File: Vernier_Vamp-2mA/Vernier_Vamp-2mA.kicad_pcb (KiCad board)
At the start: 4 copper layers, 128.5 x 99.5 mm, 185 parts, among them J1 Conn_01x02, J2 RJ45, J3 Screw_Terminal_01x04, J4 Conn_02x07_Odd_Even, J5 Conn_Coaxial, J6 Conn_Coaxial, J7 Conn_Coaxial, Q1 Si4447ADY, Q2 IRF8707PbF, SW1 DPDT_Hirose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

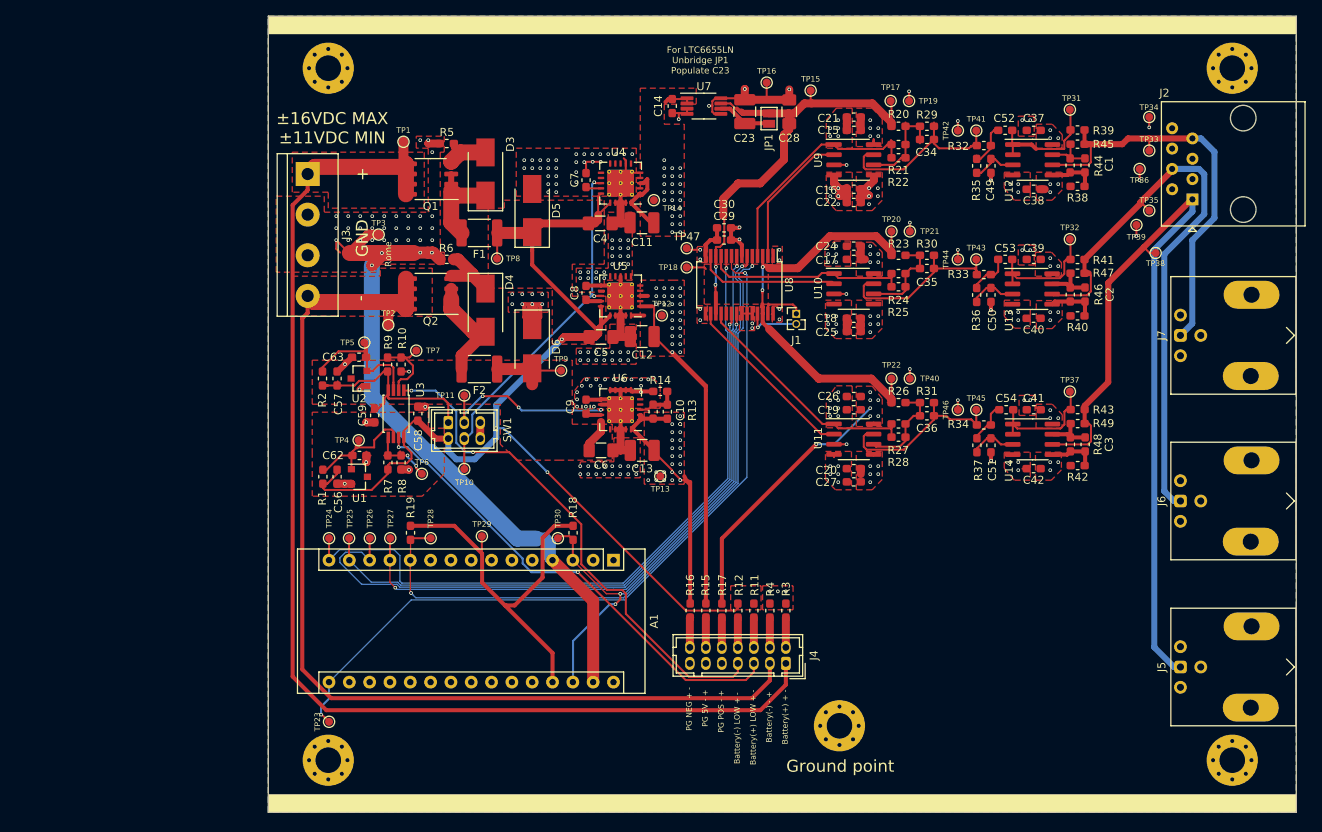
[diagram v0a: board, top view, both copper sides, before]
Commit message: Applied 1.0B changes to 2mA version
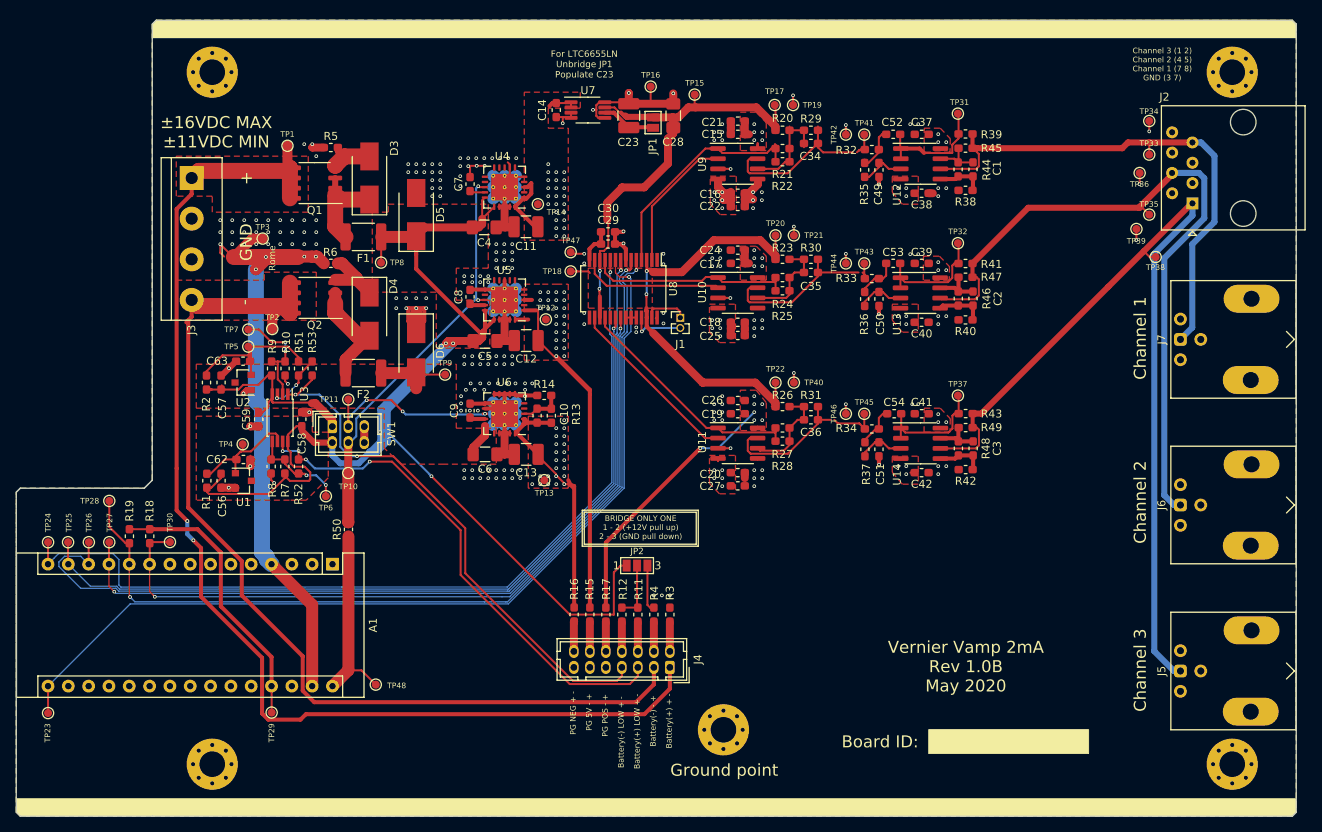
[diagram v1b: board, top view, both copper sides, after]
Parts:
- added JP2: SolderJumper_3_Open, Jumper:SolderJumper-3_P1.3mm_Open_Pad1.0x1.5mm_NumberLabels, F.Cu at (110.5, 115.3)
- added R50: 0R, Resistor_SMD:R_0603_1608Metric_Pad1.05x0.95mm_HandSolder, F.Cu at (74.4, 110.8)
- added R51: 3k, Resistor_SMD:R_0603_1608Metric_Pad1.05x0.95mm_HandSolder, F.Cu at (68.2, 90.7)
- added R52: 2M, Resistor_SMD:R_0603_1608Metric_Pad1.05x0.95mm_HandSolder, F.Cu at (68.2, 102.9)
- added R53: 133k, Resistor_SMD:R_0603_1608Metric_Pad1.05x0.95mm_HandSolder, F.Cu at (69.9, 90.7)
- added TP48: TestPoint_Probe, TestPoint:TestPoint_Pad_D1.0mm, F.Cu at (77.8, 130.2)
- J5: value Conn_Coaxial -> Channel 3
- J6: value Conn_Coaxial -> Channel 2
- J7: value Conn_Coaxial -> Channel 1
- R9: value 120k -> 133k
- moved R18 52.9 mm to (49.6, 111.7)
- moved TP30 48.5 mm to (52.1, 112.4)
- moved TP28 40.4 mm to (44.5, 107.2), turned to 0 degrees
- moved TP23 35.1 mm to (36.9, 133.8)
- moved R19 35.1 mm to (47.0, 111.7)
- moved TP27 35.1 mm to (44.5, 112.4)
- moved A1 35.1 mm to (72.4, 115.2)
- moved TP24 35.1 mm to (36.9, 112.4)
- moved TP25 35.1 mm to (39.4, 112.4)
- moved TP26 35.1 mm to (42.0, 112.4)
- moved TP29 34.3 mm to (64.8, 133.7)
- moved TP7 21.2 mm to (61.9, 85.8), turned to 180 degrees
- moved R8 16.2 mm to (64.8, 102.9)
- moved C58 14.5 mm to (68.6, 97.0)
- moved C15 14.5 mm to (123.1, 61.4)
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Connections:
- net +8V renamed +7V5
- net -8V renamed -7V5
- net /Power/+5V_c_ref renamed /Power/Battery_Management/+5V_c_ref
- net /Power/+EN renamed +12V_batt_post
- net /Power/LED1_N renamed /Power/Battery_Management/Battery+_C
- net /Power/LED2_P renamed /Power/Battery_Management/Battery-_A
- net /Power/LED3_N renamed /Power/Battery_Management/Battery+_LOW_C
- net /Power/LED3_P renamed /Power/Battery_Management/Battery+_LOW_A
- net /Power/LED4_N renamed /Power/Battery_Management/Battery-_LOW_C
- net /Power/LED4_P renamed /Power/Battery_Management/Battery-_LOW_A
- net /Power/LED5_P renamed /Power/Battery_Management/+7.5_PG_A
- net /Power/LED6_P renamed /Power/Battery_Management/+5_PG_A
- net /Power/LED7_N renamed /Power/Battery_Management/-7.5_PG_C
- A1 pad 10: Net-(A1-Pad10) -> /DAC/~RS
- A1 pad 28: /DAC/~RS -> Net-(A1-Pad28)
- A1 pad 3: /DAC/~RS -> Net-(A1-Pad3)
- C63 pad 1: /Power/-5V_c_ref -> /Power/Battery_Management/-5V_c_ref
- R11 pad 1: /Power/+12VDC_bat -> Net-(JP2-Pad2)
- R12 pad 1: /Power/+12VDC_bat -> Net-(JP2-Pad2)
- R2 pad 1: /Power/-5V_c_ref -> /Power/Battery_Management/-5V_c_ref
- TP5 pad 1: /Power/-5V_c_ref -> /Power/Battery_Management/-5V_c_ref
- U2 pad 2: /Power/-5V_c_ref -> /Power/Battery_Management/-5V_c_ref
- U3 pad 3: /Power/-5V_c_ref -> Net-(R51-Pad1)
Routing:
- net GND: track 156.2 -> 203.7 mm
- net /Power/+12VDC_bat: track 143.0 -> 172.8 mm, vias 3 -> 4
- net /DAC/~RS: track 76.1 -> 103.1 mm, vias 3 -> 2
- net Net-(A1-Pad30): track 0.00 -> 26.5 mm
- net /DAC/MSB: track 86.3 -> 111.2 mm
- net /DAC/SDO: track 78.0 -> 98.6 mm
- net /DAC/SDI: track 90.2 -> 110.8 mm
- net /DAC/~LDAC: track 75.6 -> 96.3 mm
- net /DAC/~CS: track 91.9 -> 112.5 mm
- net /Power/Battery_Management/-5V_c_ref: track 0.00 -> 18.4 mm
- net /Power/-5V_c_ref: track 18.4 -> 0.00 mm
- net /DAC/CLK: track 97.8 -> 116.0 mm, vias 2 -> 1
- net /Channel_Outputs/Coil_Iout_2: track 76.0 -> 90.0 mm
- net /Channel_Outputs/Coil_Iout_1: track 54.1 -> 68.1 mm
- net +5VD: track 47.8 -> 35.4 mm
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- added copper zone on F.Cu, net (none)
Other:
- board size 128.5 x 99.5 mm -> 160 x 99.5 mm
- board text added: "BRIDGE ONLY ONE 1 - 2 (+12V pull up) 2 - 3 (GND pull down)"
- board text added: "Board ID:"
- board text added: "Channel 1"
- board text added: "Channel 2"
- board text added: "Channel 3"
- board text added: "Channel 3 (1 2) Channel 2 (4 5) Channel 1 (7 8) GND (3 7)"
- board text added: "Vernier Vamp 2mA Rev 1.0B May 2020"
- board text added: "Vernier Vamp 2mA Rev 1.0B May 2020 Designer: Marcin Mrozowski EQOP"
- board text removed: "Vernier Vamp 200mA Rev 1.0A EQOP"

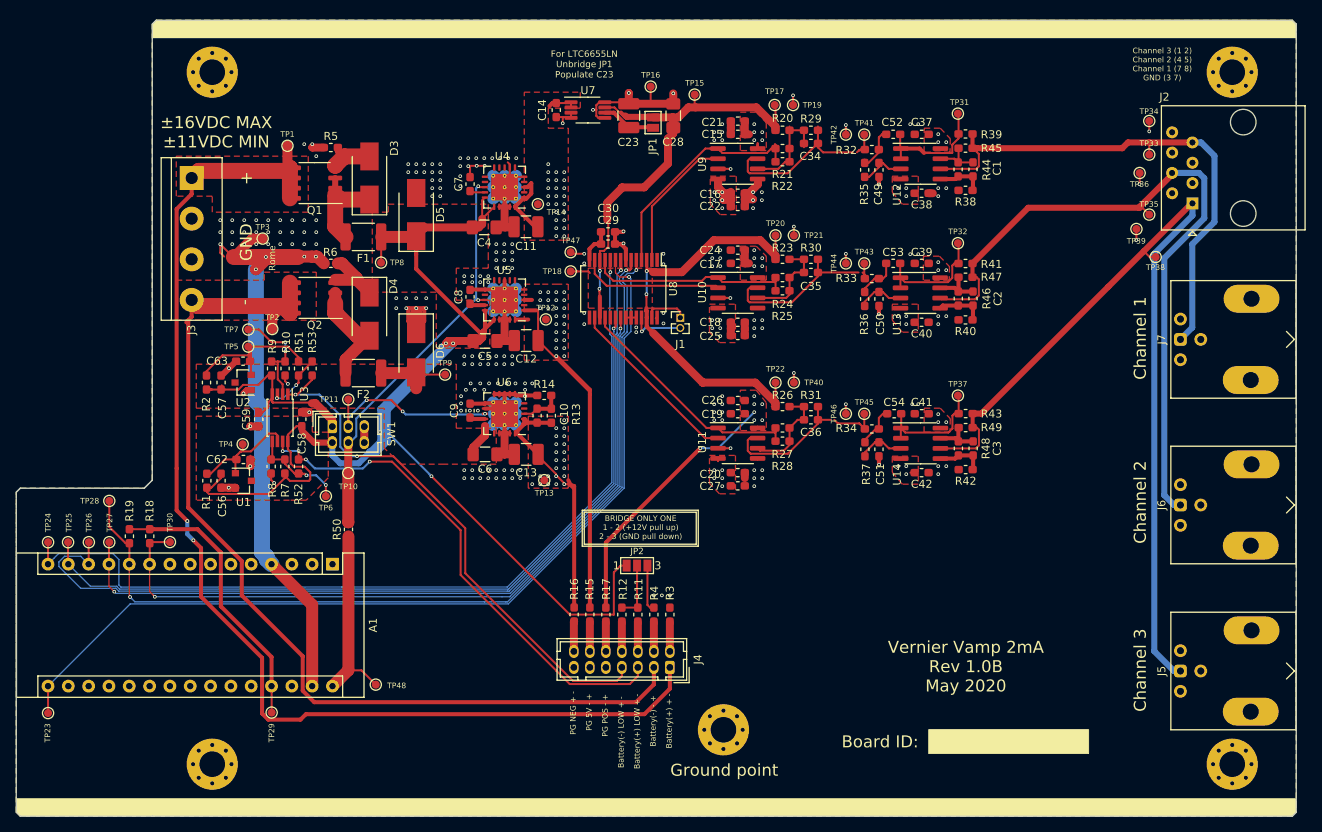
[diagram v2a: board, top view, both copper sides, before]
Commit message: 1.0C Initial commit
-Fixed amplifier output
-Changed connectors to IDC
-Via perimeter added
TODO:
Add shielding over analogue section
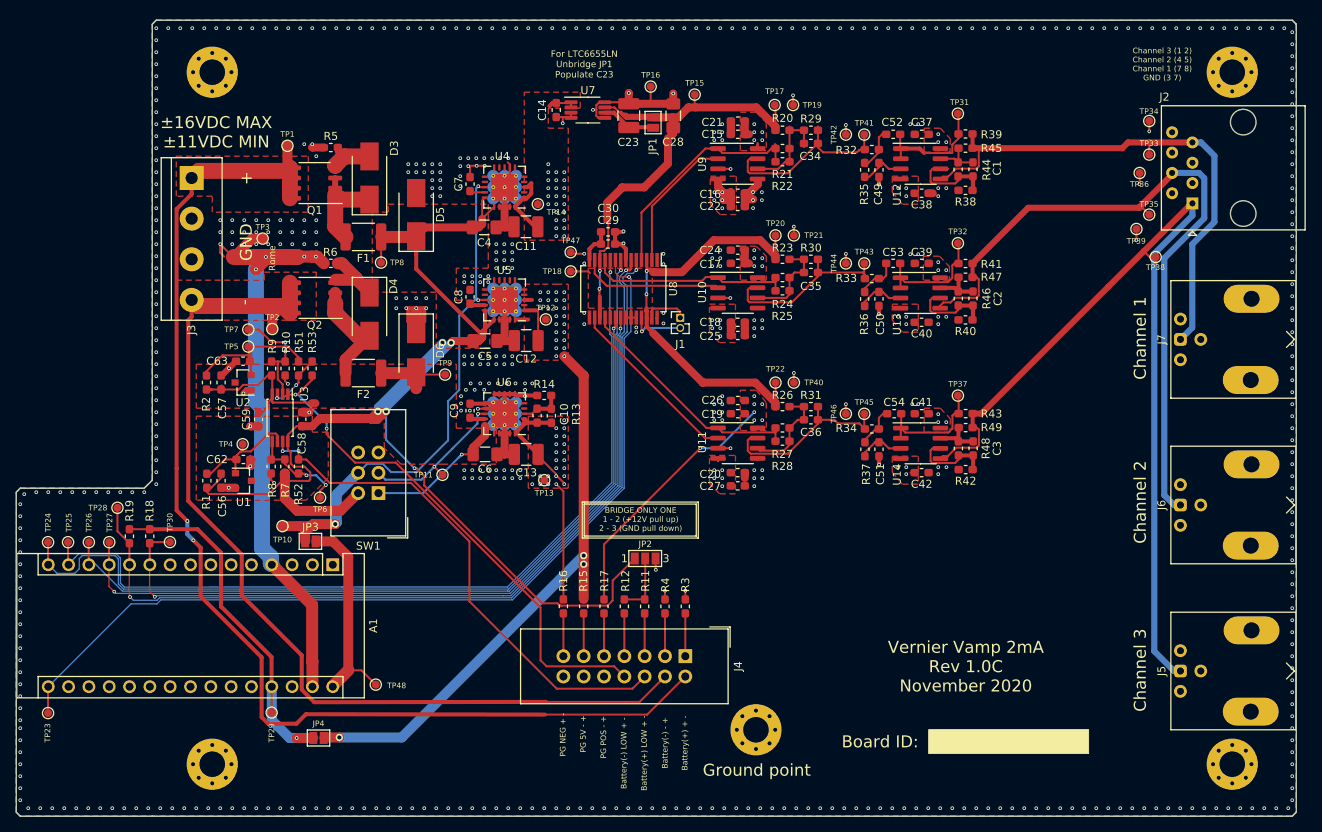
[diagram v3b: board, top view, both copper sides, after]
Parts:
- removed R50: 0R, Resistor_SMD:R_0603_1608Metric_Pad1.05x0.95mm_HandSolder
- added JP3: SolderJumper_2_Open, Jumper:SolderJumper-2_P1.3mm_Open_Pad1.0x1.5mm, F.Cu at (69.7, 112.3)
- added JP4: SolderJumper_2_Open, Jumper:SolderJumper-2_P1.3mm_Open_Pad1.0x1.5mm, F.Cu at (70.7, 136.9)
- A1: value Arduino_Nano_v3.x -> Arduino_Nano_Every
- J4: footprint Connector_Hirose:Hirose_DF11-14DP-2DSA_2x07_P2.00mm_Vertical -> Connector_IDC:IDC-Header_2x07_P2.54mm_Vertical
- SW1: footprint Connector_Hirose:Hirose_DF11-6DP-2DSA_2x03_P2.00mm_Vertical -> Connector_IDC:IDC-Header_2x03_P2.54mm_Vertical
- moved TP11 15.1 mm to (86.2, 104.0)
- moved TP10 10.6 mm to (66.2, 110.4)
- moved SW1 10.1 mm to (78.2, 106.3), turned to 180 degrees
- moved H5 4.06 mm to (125.4, 135.8)
- moved J4 2.39 mm to (116.5, 126.6), turned to 270 degrees
- moved R3 2.19 mm to (116.5, 120.4)
- moved R4 1.73 mm to (114.0, 120.4)
- moved R16 1.69 mm to (101.3, 120.4)
- moved JP2 1.35 mm to (111.5, 114.4)
- moved TP28 1.33 mm to (45.5, 108.1)
- moved R11 1.33 mm to (111.4, 120.4)
- moved R15 1.28 mm to (103.8, 120.4)
- moved R12 1.07 mm to (108.9, 120.4)
- moved R17 1.05 mm to (106.4, 120.4)
- moved TP6 0.75 mm to (70.9, 106.8)
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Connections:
- A1 pad 1: Net-(A1-Pad1) -> (no net)
- A1 pad 14: /DAC/SDO -> /DAC/SDI
- A1 pad 15: /DAC/SDI -> /DAC/SDO
- A1 pad 17: Net-(A1-Pad17) -> (no net)
- A1 pad 18: Net-(A1-Pad18) -> (no net)
- A1 pad 19: Net-(A1-Pad19) -> (no net)
- A1 pad 2: Net-(A1-Pad2) -> (no net)
- A1 pad 20: Net-(A1-Pad20) -> (no net)
- A1 pad 21: Net-(A1-Pad21) -> (no net)
- A1 pad 22: Net-(A1-Pad22) -> (no net)
- A1 pad 23: Net-(A1-Pad23) -> (no net)
- A1 pad 24: Net-(A1-Pad24) -> (no net)
- A1 pad 25: Net-(A1-Pad25) -> (no net)
- A1 pad 26: Net-(A1-Pad26) -> (no net)
- A1 pad 28: Net-(A1-Pad28) -> (no net)
- A1 pad 3: Net-(A1-Pad3) -> (no net)
- A1 pad 5: Net-(A1-Pad5) -> (no net)
- A1 pad 6: Net-(A1-Pad6) -> (no net)
- A1 pad 7: Net-(A1-Pad7) -> (no net)
- A1 pad 8: Net-(A1-Pad8) -> (no net)
- A1 pad 9: Net-(A1-Pad9) -> (no net)
- J4 pad 1: +BATT -> /Power/Battery_Management/Battery+_C
- J4 pad 10: /Power/Battery_Management/+7.5_PG_A -> GND
- J4 pad 11: GND -> /Power/Battery_Management/+5_PG_A
- J4 pad 12: /Power/Battery_Management/+5_PG_A -> GND
- J4 pad 13: GND -> /Power/Battery_Management/-7.5_PG_C
- J4 pad 14: /Power/Battery_Management/-7.5_PG_C -> GND
- J4 pad 2: /Power/Battery_Management/Battery+_C -> +BATT
- J4 pad 3: -BATT -> /Power/Battery_Management/Battery-_A
- J4 pad 4: /Power/Battery_Management/Battery-_A -> -BATT
- J4 pad 5: /Power/Battery_Management/Battery+_LOW_C -> /Power/Battery_Management/Battery+_LOW_A
- J4 pad 6: /Power/Battery_Management/Battery+_LOW_A -> /Power/Battery_Management/Battery+_LOW_C
- J4 pad 7: /Power/Battery_Management/Battery-_LOW_C -> /Power/Battery_Management/Battery-_LOW_A
- J4 pad 8: /Power/Battery_Management/Battery-_LOW_A -> /Power/Battery_Management/Battery-_LOW_C
- J4 pad 9: GND -> /Power/Battery_Management/+7.5_PG_A
- TP24 pad 1: /DAC/SDI -> /DAC/SDO
- TP25 pad 1: /DAC/SDO -> /DAC/SDI
- U12 pad 5: Net-(C1-Pad2) -> /Channel_Outputs/Coil_Iout_1
- U12 pad 6: /Channel_Outputs/Coil_Iout_1 -> Net-(C1-Pad2)
- U13 pad 5: Net-(C2-Pad2) -> /Channel_Outputs/Coil_Iout_2
- U13 pad 6: /Channel_Outputs/Coil_Iout_2 -> Net-(C2-Pad2)
- U14 pad 5: Net-(C3-Pad2) -> /Channel_Outputs/Coil_Iout_3
- U14 pad 6: /Channel_Outputs/Coil_Iout_3 -> Net-(C3-Pad2)
- U4 pad 10: Net-(U4-Pad10) -> GND
- U4 pad 11: GND -> (no net)
- U4 pad 4: Net-(U4-Pad4) -> (no net)
- U4 pad 5: GND -> (no net)
- U4 pad 6: Net-(U4-Pad6) -> GND
- U4 pad 8: Net-(U4-Pad8) -> GND
- U5 pad 10: Net-(U5-Pad10) -> GND
- U5 pad 11: GND -> (no net)
- U5 pad 12: Net-(U5-Pad12) -> (no net)
- U5 pad 4: Net-(U5-Pad4) -> (no net)
- U5 pad 5: Net-(U5-Pad5) -> (no net)
- U5 pad 8: GND -> (no net)
- U5 pad 9: Net-(U5-Pad9) -> (no net)
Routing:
- net +5V: track 57.2 -> 87.8 mm, vias 26 -> 29
- net +12V_batt_post: track 51.1 -> 65.7 mm, vias 2 -> 3
- net +5VD: track 35.4 -> 45.7 mm, vias 0 -> 1
- net GND: track 203.7 -> 193.8 mm, vias 225 -> 566
- net /Power/+12VDC_bat: track 172.8 -> 182.7 mm, vias 4 -> 5
- net /DAC/~CS: track 112.5 -> 104.0 mm
- net /DAC/SDO: track 98.6 -> 105.5 mm
- net /Power/-12VDC_bat: track 44.2 -> 50.6 mm, vias 0 -> 1
- net Net-(C1-Pad2): track 6.51 -> 12.0 mm
- net Net-(C3-Pad2): track 6.05 -> 10.6 mm
- net Net-(C2-Pad2): track 6.07 -> 10.6 mm
- net /Power/-EN: track 23.3 -> 19.2 mm, vias 3 -> 2
- net -7V5: track 40.6 -> 37.6 mm
- net /DAC/SDI: track 110.8 -> 108.3 mm
- net Net-(A1-Pad30): track 26.5 -> 28.8 mm
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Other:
- board text added: "Vernier Vamp 2mA Rev 1.0C November 2020"
- board text added: "Vernier Vamp 2mA Rev 1.0C November 2020 Designer: Marcin Mrozowski EQOP"
- board text removed: "Vernier Vamp 2mA Rev 1.0B May 2020"
- board text removed: "Vernier Vamp 2mA Rev 1.0B May 2020 Designer: Marcin Mrozowski EQOP"
